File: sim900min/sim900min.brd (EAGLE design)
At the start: 30.5 x 25.4 mm, 2 parts

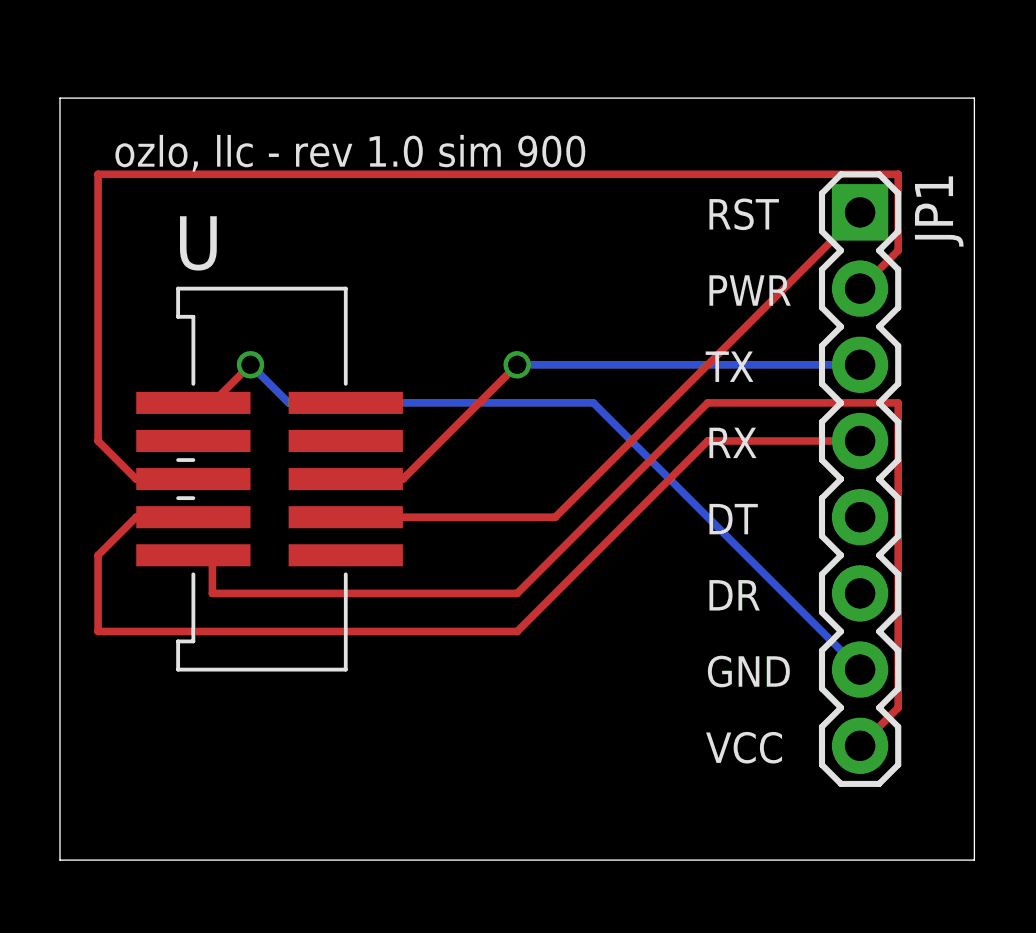
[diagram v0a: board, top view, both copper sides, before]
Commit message: redesigned sim900min for pcb production
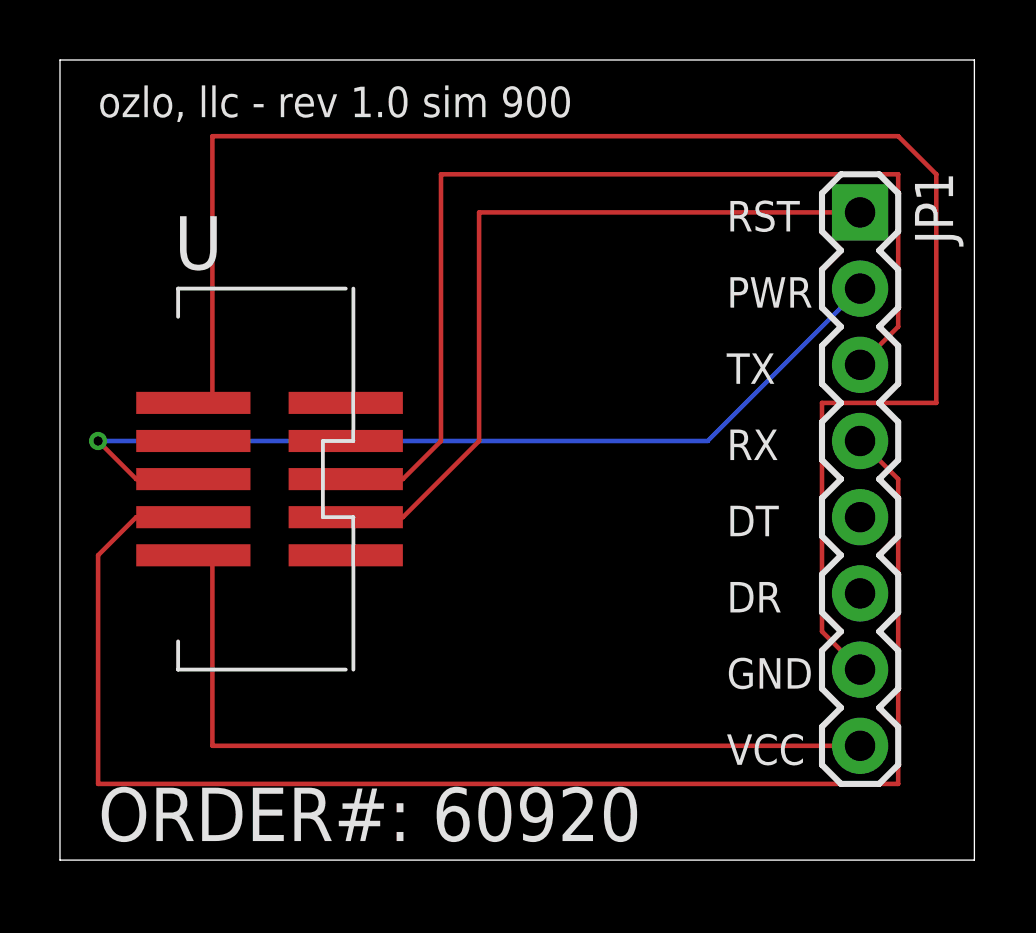
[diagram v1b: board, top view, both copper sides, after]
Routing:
- net GND: track 27.0 -> 55.0 mm, vias 1 -> 0
- net N$3: track 18.7 -> 34.7 mm, vias 1 -> 0
- net N$2: track 34.3 -> 49.9 mm
- net N$4: track 43.6 -> 31.2 mm, vias 0 -> 1
- net +5V: track 39.4 -> 28.6 mm
- net N$5: track 21.4 -> 25.8 mm
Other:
- board size 30.5 x 25.4 mm -> 30.5 x 26.7 mm
- board text added: "ORDER#: 60920"
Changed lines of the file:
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@@
 <plain>
 <wire x1="0" y1="0" x2="30.48" y2="0" width="0" layer="20"/>
-<wire x1="30.48" y1="0" x2="30.48" y2="25.4" width="0" layer="20"/>
-<wire x1="30.48" y1="25.4" x2="0" y2="25.4" width="0" layer="20"/>
-<wire x1="0" y1="25.4" x2="0" y2="0" width="0" layer="20"/>
-<text x="21.5265" y="3.2385" size="1.016" layer="121">VCC</text>
-<text x="21.5265" y="5.7785" size="1.016" layer="121">GND</text>
-<text x="21.5265" y="21.0185" size="1.016" layer="121">RST</text>
-<text x="21.5265" y="18.4785" size="1.016" layer="121">PWR</text>
-<text x="21.5265" y="15.9385" size="1.016" layer="121">TX</text>
-<text x="21.5265" y="13.3985" size="1.016" layer="121">RX</text>
-<text x="21.5265" y="10.8585" size="1.016" layer="121">DT</text>
-<text x="21.5265" y="8.3185" size="1.016" layer="121">DR</text>
-<text x="1.778" y="23.114" size="1.016" layer="121">ozlo, llc - rev 1.0 sim 900</text>
-<text x="3.81" y="19.685" size="1.778" layer="121">U</text>
+<wire x1="30.48" y1="0" x2="30.48" y2="26.67" width="0" layer="20"/>
+<wire x1="30.48" y1="26.67" x2="0" y2="26.67" width="0" layer="20"/>
+<wire x1="0" y1="26.67" x2="0" y2="0" width="0" layer="20"/>
+<text x="22.225" y="3.175" size="1.016" layer="25" font="vector">VCC</text>
+<text x="22.225" y="5.715" size="1.016" layer="25" font="vector">GND</text>
+<text x="22.225" y="20.955" size="1.016" layer="25" font="vector">RST</text>
+<text x="22.225" y="18.415" size="1.016" layer="25" font="vector">PWR</text>
+<text x="22.225" y="15.875" size="1.016" layer="25" font="vector">TX</text>
+<text x="22.225" y="13.335" size="1.016" layer="25" font="vector">RX</text>
+<text x="22.225" y="10.795" size="1.016" layer="25" font="vector">DT</text>
+<text x="22.225" y="8.255" size="1.016" layer="25" font="vector">DR</text>
+<text x="1.27" y="24.765" size="1.016" layer="25" font="vector">ozlo, llc - rev 1.0 sim 900</text>
+<text x="3.81" y="19.685" size="1.778" layer="25" font="vector">U</text>
+<text x="1.27" y="0.635" size="1.778" layer="25" font="vector">ORDER#: 60920</text>
 </plain>
 <attributes>
@@
 </autorouter>
 <elements>
+<element name="JP1" library="SparkFun-Connectors" package="1X08" value="" x="26.67" y="21.59" rot="R270"/>
 <element name="U$1" library="ozlollc" package="SHF105DSM" value="SHF105SM" x="6.985" y="12.7" rot="R180"/>
-<element name="JP1" library="SparkFun-Connectors" package="1X08" value="" x="26.67" y="21.59" rot="R270"/>
 </elements>
 <signals>
+<signal name="+5V">
+<contactref element="JP1" pad="8"/>
+<contactref element="U$1" pad="2"/>
+<wire x1="5.08" y1="3.81" x2="26.67" y2="3.81" width="0.1524" layer="1"/>
+<wire x1="5.08" y1="10.16" x2="5.08" y2="3.81" width="0.1524" layer="1"/>
+<wire x1="5.08" y1="10.16" x2="4.445" y2="10.16" width="0.1524" layer="1"/>
+</signal>
+<signal name="GND">
+<contactref element="JP1" pad="7"/>
+<contactref element="U$1" pad="10"/>
+<wire x1="25.4" y1="7.62" x2="26.67" y2="6.35" width="0.1524" layer="1"/>
+<wire x1="25.4" y1="15.24" x2="25.4" y2="7.62" width="0.1524" layer="1"/>
+<wire x1="29.21" y1="15.24" x2="25.4" y2="15.24" width="0.1524" layer="1"/>
+<wire x1="29.21" y1="22.86" x2="29.21" y2="15.24" width="0.1524" layer="1"/>
+<wire x1="27.94" y1="24.13" x2="29.21" y2="22.86" width="0.1524" layer="1"/>
+<wire x1="5.08" y1="24.13" x2="27.94" y2="24.13" width="0.1524" layer="1"/>
+<wire x1="5.08" y1="15.24" x2="5.08" y2="24.13" width="0.1524" layer="1"/>
+<wire x1="5.08" y1="15.24" x2="4.445" y2="15.24" width="0.1524" layer="1"/>
+</signal>
+<signal name="N$2">
+<contactref element="JP1" pad="4"/>
+<contactref element="U$1" pad="4"/>
+<wire x1="27.94" y1="12.7" x2="26.67" y2="13.97" width="0.1524" layer="1"/>
+<wire x1="27.94" y1="2.54" x2="27.94" y2="12.7" width="0.1524" layer="1"/>
+<wire x1="1.27" y1="2.54" x2="27.94" y2="2.54" width="0.1524" layer="1"/>
+<wire x1="1.27" y1="10.16" x2="1.27" y2="2.54" width="0.1524" layer="1"/>
+<wire x1="2.54" y1="11.43" x2="1.27" y2="10.16" width="0.1524" layer="1"/>
+<wire x1="3.81" y1="11.43" x2="2.54" y2="11.43" width="0.1524" layer="1"/>
+<wire x1="3.81" y1="11.43" x2="4.445" y2="11.43" width="0.1524" layer="1"/>
+</signal>
+<signal name="N$3">
+<contactref element="JP1" pad="3"/>
+<contactref element="U$1" pad="5"/>
+<wire x1="27.94" y1="17.78" x2="26.67" y2="16.51" width="0.1524" layer="1"/>
+<wire x1="27.94" y1="22.86" x2="27.94" y2="17.78" width="0.1524" layer="1"/>
+<wire x1="12.7" y1="22.86" x2="27.94" y2="22.86" width="0.1524" layer="1"/>
+<wire x1="12.7" y1="13.97" x2="12.7" y2="22.86" width="0.1524" layer="1"/>
+<wire x1="11.43" y1="12.7" x2="12.7" y2="13.97" width="0.1524" layer="1"/>
+<wire x1="10.16" y1="12.7" x2="11.43" y2="12.7" width="0.1524" layer="1"/>
+<wire x1="10.16" y1="12.7" x2="9.525" y2="12.7" width="0.1524" layer="1"/>
+</signal>
+<signal name="N$4">
+<contactref element="JP1" pad="2"/>
+<contactref element="U$1" pad="6"/>
+<wire x1="21.59" y1="13.97" x2="26.67" y2="19.05" width="0.1524" layer="16"/>
+<wire x1="1.27" y1="13.97" x2="21.59" y2="13.97" width="0.1524" layer="16"/>
+<wire x1="2.54" y1="12.7" x2="1.27" y2="13.97" width="0.1524" layer="1"/>
+<wire x1="3.81" y1="12.7" x2="2.54" y2="12.7" width="0.1524" layer="1"/>
+<wire x1="3.81" y1="12.7" x2="4.445" y2="12.7" width="0.1524" layer="1"/>
+<via x="1.27" y="13.97" extent="1-16" drill="0.3048"/>
+</signal>
+<signal name="N$5">
+<contactref element="JP1" pad="1"/>
+<contactref element="U$1" pad="3"/>
+<wire x1="13.97" y1="21.59" x2="26.67" y2="21.59" width="0.1524" layer="1"/>
+<wire x1="13.97" y1="13.97" x2="13.97" y2="21.59" width="0.1524" layer="1"/>
+<wire x1="11.43" y1="11.43" x2="13.97" y2="13.97" width="0.1524" layer="1"/>
+<wire x1="10.16" y1="11.43" x2="11.43" y2="11.43" width="0.1524" layer="1"/>
+<wire x1="10.16" y1="11.43" x2="9.525" y2="11.43" width="0.1524" layer="1"/>
+</signal>
 <signal name="+3V3">
 <contactref element="U$1" pad="1"/>
 </signal>
-<signal name="+5V">
-<contactref element="U$1" pad="2"/>
-<contactref element="JP1" pad="8"/>
-<wire x1="27.94" y1="5.08" x2="26.67" y2="3.81" width="0.254" layer="1"/>
-<wire x1="27.94" y1="15.24" x2="27.94" y2="5.08" width="0.254" layer="1"/>
-<wire x1="21.59" y1="15.24" x2="27.94" y2="15.24" width="0.254" layer="1"/>
-<wire x1="15.24" y1="8.89" x2="21.59" y2="15.24" width="0.254" layer="1"/>
-<wire x1="5.08" y1="8.89" x2="15.24" y2="8.89" width="0.254" layer="1"/>
-<wire x1="5.08" y1="10.16" x2="5.08" y2="8.89" width="0.254" layer="1"/>
-<wire x1="5.08" y1="10.16" x2="4.445" y2="10.16" width="0.254" layer="1"/>
-</signal>
-<signal name="GND">
-<contactref element="U$1" pad="10"/>
-<contactref element="JP1" pad="7"/>
-<wire x1="17.78" y1="15.24" x2="26.67" y2="6.35" width="0.254" layer="16"/>
-<wire x1="7.62" y1="15.24" x2="17.78" y2="15.24" width="0.254" layer="16"/>
-<wire x1="6.35" y1="16.51" x2="7.62" y2="15.24" width="0.254" layer="16"/>
-<wire x1="5.08" y1="15.24" x2="6.35" y2="16.51" width="0.254" layer="1"/>
-<wire x1="5.08" y1="15.24" x2="4.445" y2="15.24" width="0.254" layer="1"/>
-<via x="6.35" y="16.51" extent="1-16" drill="0.6096"/>
-</signal>
-<signal name="N$2">
-<contactref element="U$1" pad="4"/>
-<contactref element="JP1" pad="4"/>
-<wire x1="21.59" y1="13.97" x2="26.67" y2="13.97" width="0.254" layer="1"/>
-<wire x1="15.24" y1="7.62" x2="21.59" y2="13.97" width="0.254" layer="1"/>
-<wire x1="1.27" y1="7.62" x2="15.24" y2="7.62" width="0.254" layer="1"/>
-<wire x1="1.27" y1="10.16" x2="1.27" y2="7.62" width="0.254" layer="1"/>
-<wire x1="2.54" y1="11.43" x2="1.27" y2="10.16" width="0.254" layer="1"/>
-<wire x1="3.81" y1="11.43" x2="2.54" y2="11.43" width="0.254" layer="1"/>
-<wire x1="3.81" y1="11.43" x2="4.445" y2="11.43" width="0.254" layer="1"/>
-</signal>
-<signal name="N$3">
-<contactref element="U$1" pad="5"/>
-<contactref element="JP1" pad="3"/>
-<wire x1="15.24" y1="16.51" x2="26.67" y2="16.51" width="0.254" layer="16"/>
-<wire x1="11.43" y1="12.7" x2="15.24" y2="16.51" width="0.254" layer="1"/>
-<wire x1="10.16" y1="12.7" x2="11.43" y2="12.7" width="0.254" layer="1"/>
-<wire x1="10.16" y1="12.7" x2="9.525" y2="12.7" width="0.254" layer="1"/>
-<via x="15.24" y="16.51" extent="1-16" drill="0.6096"/>
-</signal>
-<signal name="N$4">
-<contactref element="U$1" pad="6"/>
-<contactref element="JP1" pad="2"/>
-<wire x1="27.94" y1="20.32" x2="26.67" y2="19.05" width="0.254" layer="1"/>
-<wire x1="27.94" y1="22.86" x2="27.94" y2="20.32" width="0.254" layer="1"/>
-<wire x1="1.27" y1="22.86" x2="27.94" y2="22.86" width="0.254" layer="1"/>
-<wire x1="1.27" y1="13.97" x2="1.27" y2="22.86" width="0.254" layer="1"/>
-<wire x1="2.54" y1="12.7" x2="1.27" y2="13.97" width="0.254" layer="1"/>
-<wire x1="3.81" y1="12.7" x2="2.54" y2="12.7" width="0.254" layer="1"/>
-<wire x1="3.81" y1="12.7" x2="4.445" y2="12.7" width="0.254" layer="1"/>
-</signal>
-<signal name="N$5">
-<contactref element="U$1" pad="3"/>
-<contactref element="JP1" pad="1"/>
-<wire x1="16.51" y1="11.43" x2="26.67" y2="21.59" width="0.254" layer="1"/>
-<wire x1="10.16" y1="11.43" x2="16.51" y2="11.43" width="0.254" layer="1"/>
-<wire x1="10.16" y1="11.43" x2="9.525" y2="11.43" width="0.254" layer="1"/>
-</signal>
 </signals>
